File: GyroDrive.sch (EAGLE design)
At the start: 43 parts, among them IC1 AD8235, IC2 AD8235, IC3 AD8235, IC4 AD8235

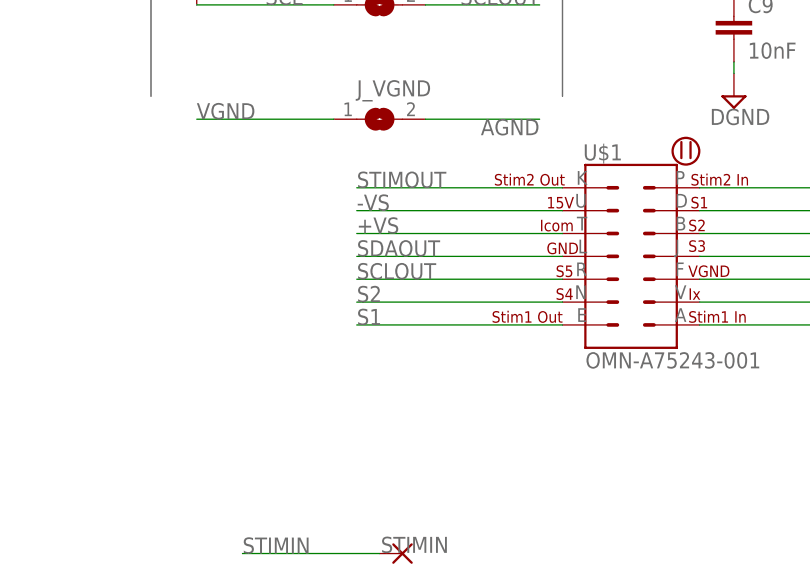
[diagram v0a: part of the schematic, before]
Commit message: Changed pinout to group digital signals closer together
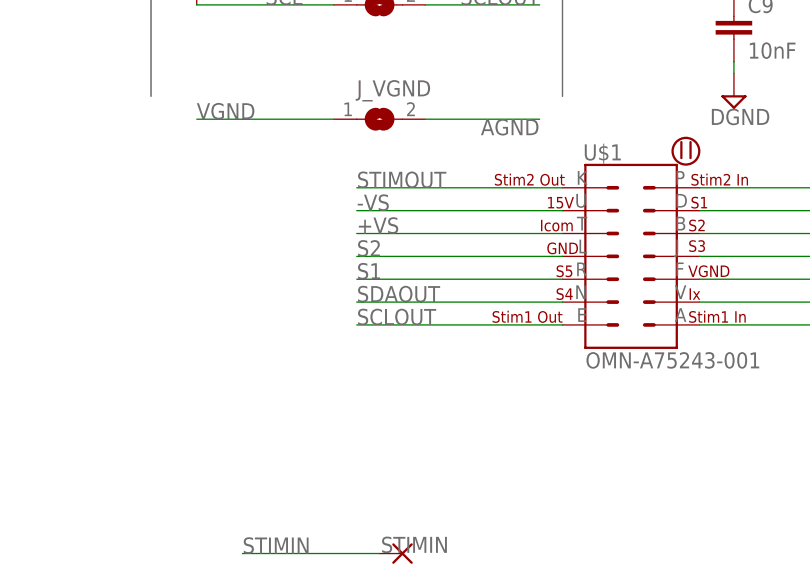
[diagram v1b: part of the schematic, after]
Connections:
- net S1: now also U$1.R; no longer U$1.E
- net S2: now also U$1.L; no longer U$1.N
- net SCLOUT: now also U$1.E; no longer U$1.R
- net SDAOUT: now also U$1.N; no longer U$1.L
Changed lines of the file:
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@@
 </segment>
 <segment>
-<pinref part="U$1" gate="G$1" pin="E"/>
-<wire x1="137.16" y1="40.64" x2="114.3" y2="40.64" width="0.1524" layer="91"/>
-<label x="114.3" y="40.64" size="1.778" layer="95"/>
+<pinref part="U$1" gate="G$1" pin="R"/>
+<wire x1="137.16" y1="45.72" x2="114.3" y2="45.72" width="0.1524" layer="91"/>
+<label x="114.3" y="45.72" size="1.778" layer="95"/>
 </segment>
 </net>
@@
 </segment>
 <segment>
-<pinref part="U$1" gate="G$1" pin="N"/>
-<wire x1="137.16" y1="43.18" x2="114.3" y2="43.18" width="0.1524" layer="91"/>
-<label x="114.3" y="43.18" size="1.778" layer="95"/>
+<pinref part="U$1" gate="G$1" pin="L"/>
+<wire x1="137.16" y1="48.26" x2="114.3" y2="48.26" width="0.1524" layer="91"/>
+<label x="114.3" y="48.26" size="1.778" layer="95"/>
 </segment>
 </net>
@@
 </segment>
 <segment>
-<pinref part="U$1" gate="G$1" pin="L"/>
-<wire x1="137.16" y1="48.26" x2="114.3" y2="48.26" width="0.1524" layer="91"/>
-<label x="114.3" y="48.26" size="1.778" layer="95"/>
+<pinref part="U$1" gate="G$1" pin="N"/>
+<wire x1="137.16" y1="43.18" x2="114.3" y2="43.18" width="0.1524" layer="91"/>
+<label x="114.3" y="43.18" size="1.778" layer="95"/>
 </segment>
 </net>
@@
 </segment>
 <segment>
-<pinref part="U$1" gate="G$1" pin="R"/>
-<wire x1="137.16" y1="45.72" x2="114.3" y2="45.72" width="0.1524" layer="91"/>
-<label x="114.3" y="45.72" size="1.778" layer="95"/>
-</segment>
-</net>
+<pinref part="U$1" gate="G$1" pin="E"/>
+<wire x1="137.16" y1="40.64" x2="114.3" y2="40.64" width="0.1524" layer="91"/>
+<label x="114.3" y="40.64" size="1.778" layer="95"/>
+</segment>
+</net>

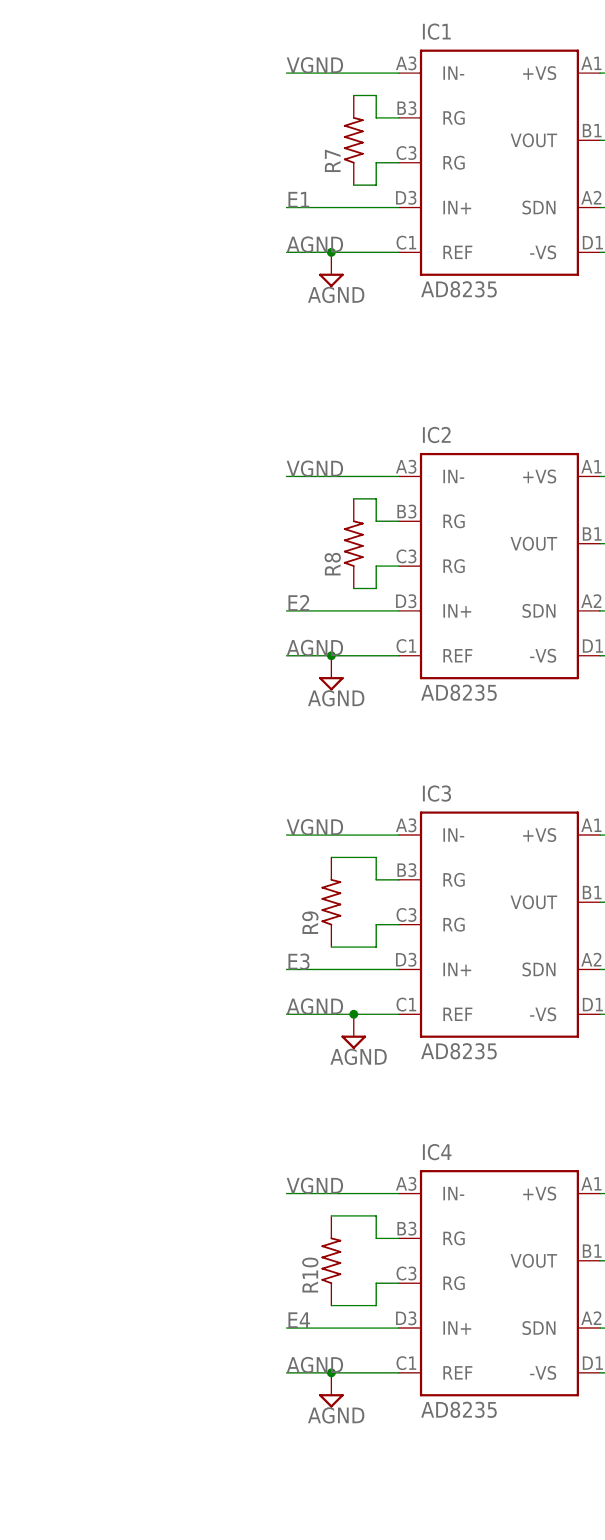
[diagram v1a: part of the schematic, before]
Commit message: Added high pass filters in front of inputs to in-amps
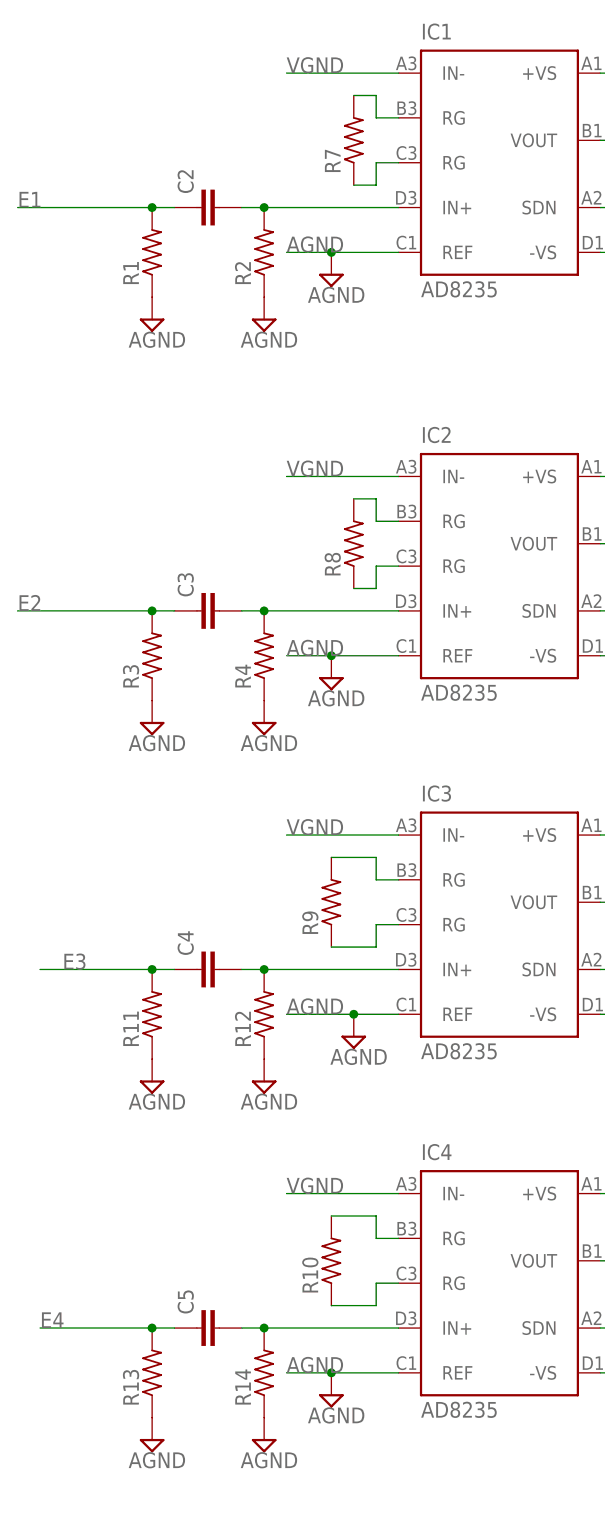
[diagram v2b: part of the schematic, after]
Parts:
- added C2, C3, C4, C5: (no value), resistor:C-EUC0201
- added R1, R11, R12, R13, R14, R2, R3, R4: (no value), resistor:R-US_R0201
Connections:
- new net N$4: C4.2, IC3.IN+, R12.2
- new net N$6: C2.2, IC1.IN+, R2.2
- new net N$8: C5.2, IC4.IN+, R14.2
- new net N$9: C3.2, IC2.IN+, R4.2
- net AGND: now also R1.1, R11.1, R12.1, R13.1, R14.1, R2.1, R3.1, R4.1
- net E1: now also C2.1, R1.2; no longer IC1.IN+
- net E2: now also C3.1, R3.2; no longer IC2.IN+
- net E3: now also C4.1, R11.2; no longer IC3.IN+
- net E4: now also C5.1, R13.2; no longer IC4.IN+
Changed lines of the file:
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@@
 <part name="C1" library="resistor" deviceset="C-EU" device="C0201"/>
 <part name="SUPPLY3" library="supply2" deviceset="DGND" device=""/>
+<part name="R1" library="resistor" deviceset="R-US_" device="R0201"/>
+<part name="C2" library="resistor" deviceset="C-EU" device="C0201"/>
+<part name="R2" library="resistor" deviceset="R-US_" device="R0201"/>
+<part name="SUPPLY4" library="supply2" deviceset="AGND" device=""/>
+<part name="SUPPLY5" library="supply2" deviceset="AGND" device=""/>
+<part name="R3" library="resistor" deviceset="R-US_" device="R0201"/>
+<part name="C3" library="resistor" deviceset="C-EU" device="C0201"/>
+<part name="R4" library="resistor" deviceset="R-US_" device="R0201"/>
+<part name="SUPPLY6" library="supply2" deviceset="AGND" device=""/>
+<part name="SUPPLY7" library="supply2" deviceset="AGND" device=""/>
+<part name="R11" library="resistor" deviceset="R-US_" device="R0201"/>
+<part name="C4" library="resistor" deviceset="C-EU" device="C0201"/>
+<part name="R12" library="resistor" deviceset="R-US_" device="R0201"/>
+<part name="SUPPLY8" library="supply2" deviceset="AGND" device=""/>
+<part name="SUPPLY9" library="supply2" deviceset="AGND" device=""/>
+<part name="R13" library="resistor" deviceset="R-US_" device="R0201"/>
+<part name="C5" library="resistor" deviceset="C-EU" device="C0201"/>
+<part name="R14" library="resistor" deviceset="R-US_" device="R0201"/>
+<part name="SUPPLY10" library="supply2" deviceset="AGND" device=""/>
+<part name="SUPPLY11" library="supply2" deviceset="AGND" device=""/>
 </parts>
 <sheets>
@@
 <instance part="C1" gate="G$1" x="104.14" y="106.68" rot="R90"/>
 <instance part="SUPPLY3" gate="G$1" x="109.22" y="104.14"/>
+<instance part="R1" gate="G$1" x="-7.62" y="144.78" rot="R90"/>
+<instance part="C2" gate="G$1" x="-2.54" y="149.86" rot="R90"/>
+<instance part="R2" gate="G$1" x="5.08" y="144.78" rot="R90"/>
+<instance part="SUPPLY4" gate="G$1" x="-7.62" y="137.16"/>
+<instance part="SUPPLY5" gate="G$1" x="5.08" y="137.16"/>
+<instance part="R3" gate="G$1" x="-7.62" y="99.06" rot="R90"/>
+<instance part="C3" gate="G$1" x="-2.54" y="104.14" rot="R90"/>
+<instance part="R4" gate="G$1" x="5.08" y="99.06" rot="R90"/>
+<instance part="SUPPLY6" gate="G$1" x="-7.62" y="91.44"/>
+<instance part="SUPPLY7" gate="G$1" x="5.08" y="91.44"/>
+<instance part="R11" gate="G$1" x="-7.62" y="58.42" rot="R90"/>
+<instance part="C4" gate="G$1" x="-2.54" y="63.5" rot="R90"/>
+<instance part="R12" gate="G$1" x="5.08" y="58.42" rot="R90"/>
+<instance part="SUPPLY8" gate="G$1" x="-7.62" y="50.8"/>
+<instance part="SUPPLY9" gate="G$1" x="5.08" y="50.8"/>
+<instance part="R13" gate="G$1" x="-7.62" y="17.78" rot="R90"/>
+<instance part="C5" gate="G$1" x="-2.54" y="22.86" rot="R90"/>
+<instance part="R14" gate="G$1" x="5.08" y="17.78" rot="R90"/>
+<instance part="SUPPLY10" gate="G$1" x="-7.62" y="10.16"/>
+<instance part="SUPPLY11" gate="G$1" x="5.08" y="10.16"/>
 </instances>
 <busses>
@@
 <wire x1="152.4" y1="53.34" x2="172.72" y2="53.34" width="0.1524" layer="91"/>
 <label x="170.18" y="53.34" size="1.778" layer="95"/>
+</segment>
+<segment>
+<pinref part="R1" gate="G$1" pin="1"/>
+<pinref part="SUPPLY4" gate="G$1" pin="AGND"/>
+</segment>
+<segment>
+<pinref part="R2" gate="G$1" pin="1"/>
+<pinref part="SUPPLY5" gate="G$1" pin="AGND"/>
+</segment>
+<segment>
+<pinref part="R3" gate="G$1" pin="1"/>
+<pinref part="SUPPLY6" gate="G$1" pin="AGND"/>
+</segment>
+<segment>
+<pinref part="R4" gate="G$1" pin="1"/>
+<pinref part="SUPPLY7" gate="G$1" pin="AGND"/>
+</segment>
+<segment>
+<pinref part="R11" gate="G$1" pin="1"/>
+<pinref part="SUPPLY8" gate="G$1" pin="AGND"/>
+</segment>
+<segment>
+<pinref part="R12" gate="G$1" pin="1"/>
+<pinref part="SUPPLY9" gate="G$1" pin="AGND"/>
+</segment>
+<segment>
+<pinref part="R13" gate="G$1" pin="1"/>
+<pinref part="SUPPLY10" gate="G$1" pin="AGND"/>
+</segment>
+<segment>
+<pinref part="R14" gate="G$1" pin="1"/>
+<pinref part="SUPPLY11" gate="G$1" pin="AGND"/>
 </segment>
 </net>
@@
 <net name="E1" class="0">
 <segment>
-<pinref part="IC1" gate="G$1" pin="IN+"/>
-<wire x1="20.32" y1="149.86" x2="7.62" y2="149.86" width="0.1524" layer="91"/>
-<label x="7.62" y="149.86" size="1.778" layer="95"/>
-</segment>
-<segment>
 <pinref part="E1" gate="1" pin="P"/>
 <wire x1="99.06" y1="177.8" x2="114.3" y2="177.8" width="0.1524" layer="91"/>
 <label x="111.76" y="177.8" size="1.778" layer="95"/>
 </segment>
+<segment>
+<pinref part="C2" gate="G$1" pin="1"/>
+<pinref part="R1" gate="G$1" pin="2"/>
+<wire x1="-5.08" y1="149.86" x2="-7.62" y2="149.86" width="0.1524" layer="91"/>
+<wire x1="-7.62" y1="149.86" x2="-22.86" y2="149.86" width="0.1524" layer="91"/>
+<junction x="-7.62" y="149.86"/>
+<label x="-22.86" y="149.86" size="1.778" layer="95"/>
+</segment>
 </net>
 <net name="E2" class="0">
-<segment>
-<pinref part="IC2" gate="G$1" pin="IN+"/>
-<wire x1="20.32" y1="104.14" x2="7.62" y2="104.14" width="0.1524" layer="91"/>
-<label x="7.62" y="104.14" size="1.778" layer="95"/>
-</segment>
 <segment>
 <wire x1="99.06" y1="170.18" x2="114.3" y2="170.18" width="0.1524" layer="91"/>
@@
 <pinref part="E2" gate="1" pin="P"/>
 </segment>
+<segment>
+<pinref part="C3" gate="G$1" pin="1"/>
+<pinref part="R3" gate="G$1" pin="2"/>
+<wire x1="-5.08" y1="104.14" x2="-7.62" y2="104.14" width="0.1524" layer="91"/>
+<wire x1="-7.62" y1="104.14" x2="-22.86" y2="104.14" width="0.1524" layer="91"/>
+<junction x="-7.62" y="104.14"/>
+<label x="-22.86" y="104.14" size="1.778" layer="95"/>
+</segment>
 </net>
 <net name="E3" class="0">
-<segment>
-<pinref part="IC3" gate="G$1" pin="IN+"/>
-<wire x1="20.32" y1="63.5" x2="7.62" y2="63.5" width="0.1524" layer="91"/>
-<label x="7.62" y="63.5" size="1.778" layer="95"/>
-</segment>
 <segment>
 <wire x1="99.06" y1="160.02" x2="114.3" y2="160.02" width="0.1524" layer="91"/>
@@
 <pinref part="E3" gate="1" pin="P"/>
 </segment>
+<segment>
+<pinref part="C4" gate="G$1" pin="1"/>
+<pinref part="R11" gate="G$1" pin="2"/>
+<wire x1="-5.08" y1="63.5" x2="-7.62" y2="63.5" width="0.1524" layer="91"/>
+<wire x1="-7.62" y1="63.5" x2="-20.32" y2="63.5" width="0.1524" layer="91"/>
+<junction x="-7.62" y="63.5"/>
+<label x="-17.78" y="63.5" size="1.778" layer="95"/>
+</segment>
 </net>
 <net name="E4" class="0">
-<segment>
-<pinref part="IC4" gate="G$1" pin="IN+"/>
-<wire x1="20.32" y1="22.86" x2="7.62" y2="22.86" width="0.1524" layer="91"/>
-<label x="7.62" y="22.86" size="1.778" layer="95"/>
-</segment>
 <segment>
 <wire x1="99.06" y1="149.86" x2="114.3" y2="149.86" width="0.1524" layer="91"/>
 <label x="111.76" y="149.86" size="1.778" layer="95"/>
 <pinref part="E4" gate="1" pin="P"/>
+</segment>
+<segment>
+<pinref part="C5" gate="G$1" pin="1"/>
+<pinref part="R13" gate="G$1" pin="2"/>
+<wire x1="-5.08" y1="22.86" x2="-7.62" y2="22.86" width="0.1524" layer="91"/>
+<wire x1="-7.62" y1="22.86" x2="-20.32" y2="22.86" width="0.1524" layer="91"/>
+<junction x="-7.62" y="22.86"/>
+<label x="-20.32" y="22.86" size="1.778" layer="95"/>
 </segment>
 </net>
@@
 </segment>
 </net>
+<net name="N$6" class="0">
+<segment>
+<pinref part="IC1" gate="G$1" pin="IN+"/>
+<pinref part="R2" gate="G$1" pin="2"/>
+<wire x1="20.32" y1="149.86" x2="5.08" y2="149.86" width="0.1524" layer="91"/>
+<pinref part="C2" gate="G$1" pin="2"/>
+<wire x1="5.08" y1="149.86" x2="2.54" y2="149.86" width="0.1524" layer="91"/>
+<junction x="5.08" y="149.86"/>
+</segment>
+</net>
+<net name="N$8" class="0">
+<segment>
+<pinref part="IC4" gate="G$1" pin="IN+"/>
+<pinref part="R14" gate="G$1" pin="2"/>
+<wire x1="20.32" y1="22.86" x2="5.08" y2="22.86" width="0.1524" layer="91"/>
+<pinref part="C5" gate="G$1" pin="2"/>
+<wire x1="5.08" y1="22.86" x2="2.54" y2="22.86" width="0.1524" layer="91"/>
+<junction x="5.08" y="22.86"/>
+</segment>
+</net>
+<net name="N$9" class="0">
+<segment>
+<pinref part="IC2" gate="G$1" pin="IN+"/>
+<pinref part="R4" gate="G$1" pin="2"/>
+<wire x1="20.32" y1="104.14" x2="5.08" y2="104.14" width="0.1524" layer="91"/>
+<pinref part="C3" gate="G$1" pin="2"/>
+<wire x1="5.08" y1="104.14" x2="2.54" y2="104.14" width="0.1524" layer="91"/>
+<junction x="5.08" y="104.14"/>
+</segment>
+</net>
+<net name="N$4" class="0">
+<segment>
+<pinref part="IC3" gate="G$1" pin="IN+"/>
+<pinref part="R12" gate="G$1" pin="2"/>
+<wire x1="20.32" y1="63.5" x2="5.08" y2="63.5" width="0.1524" layer="91"/>
+<pinref part="C4" gate="G$1" pin="2"/>
+<wire x1="2.54" y1="63.5" x2="5.08" y2="63.5" width="0.1524" layer="91"/>
+<junction x="5.08" y="63.5"/>
+</segment>
+</net>
